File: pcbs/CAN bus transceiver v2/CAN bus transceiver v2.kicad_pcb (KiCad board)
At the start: 2 copper layers, 19.8 x 16 mm, 3 parts, among them P1 CONN_01X05, P2 CONN_01X02, U1 TCAN337GDR

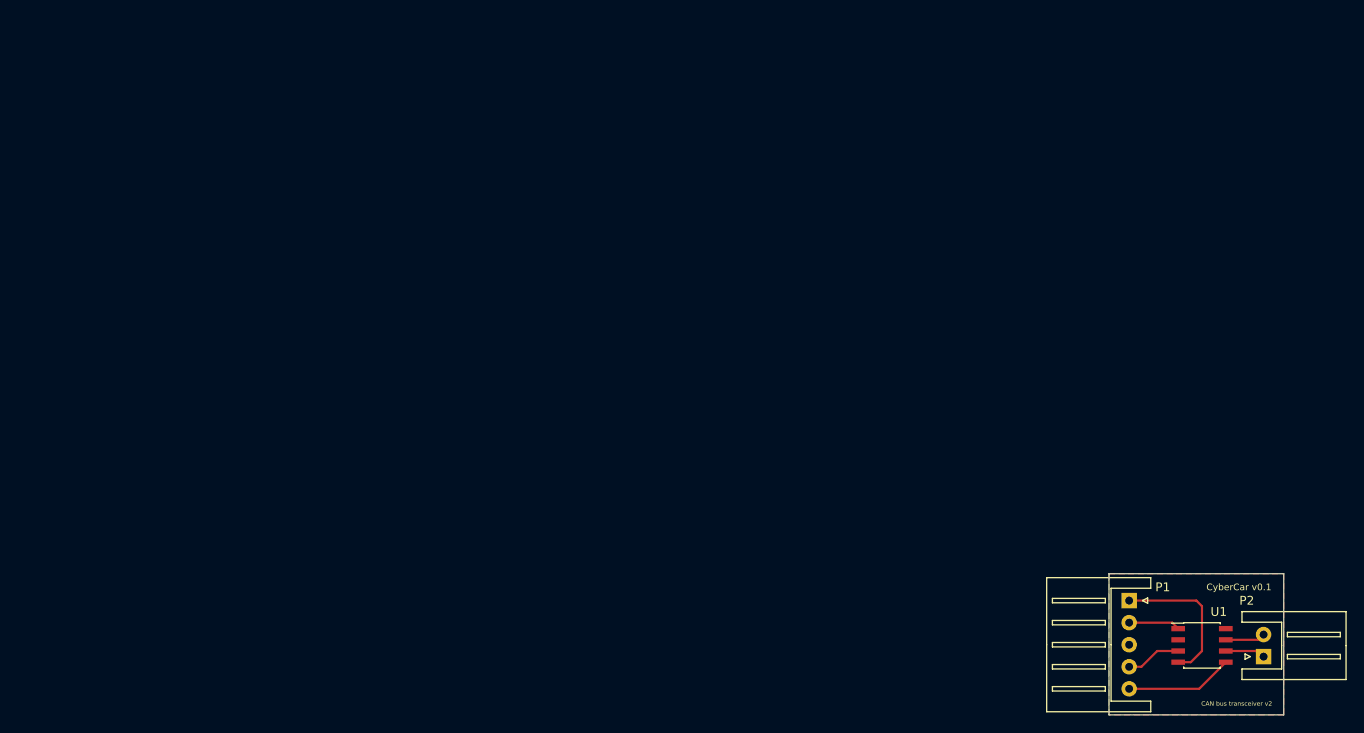
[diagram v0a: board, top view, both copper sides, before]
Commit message: added CAN bus transceiver
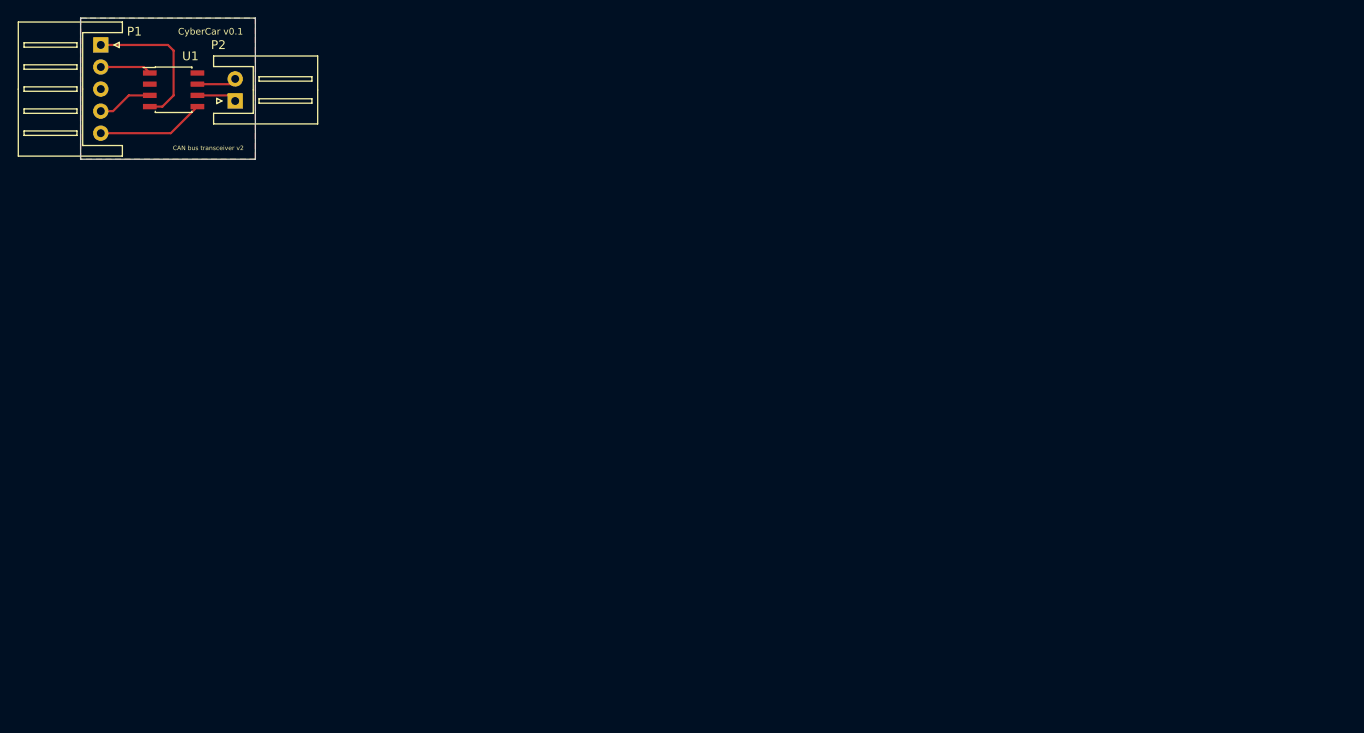
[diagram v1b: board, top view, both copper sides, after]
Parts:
- moved P1 132.5 mm to (29.5, 27.2)
- moved U1 132.5 mm to (37.7, 32.3)
- moved P2 132.5 mm to (44.7, 33.5)
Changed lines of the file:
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@@
     (links 8)
     (no_connects 0)
-    (area 134.775 86.994999 172.665 103.345001)
+    (area 18.189 16.35 65 40.353001)
     (thickness 1.6)
-    (drawings 13)
+    (drawings 15)
     (tracks 16)
     (zones 0)
@@
       (psnegative false)
       (psa4output false)
-      (plotreference true)
+      (plotreference false)
       (plotvalue false)
       (plotinvisibletext false)
@@
   )
   (module Connectors_JST:JST_XH_S05B-XH-A_05x2.50mm_Angled (layer F.Cu)
-    (at 146.05 90.17 270)
+    (at 29.464 27.178 270)
     (descr "JST XH series connector, S05B-XH-A, side entry type, through hole")
     (tags "connector jst xh tht side horizontal angled 2.50mm")
@@
   )
   (module Connectors_JST:JST_XH_S02B-XH-A_02x2.50mm_Angled (layer F.Cu)
-    (at 161.29 96.52 90)
+    (at 44.704 33.528 90)
     (descr "JST XH series connector, S02B-XH-A, side entry type, through hole")
     (tags "connector jst xh tht side horizontal angled 2.50mm")
@@
   )
   (module Housings_SOIC:SOIC-8_3.9x4.9mm_Pitch1.27mm (layer F.Cu)
-    (at 154.305 95.25)
+    (at 37.719 32.258)
     (descr "8-Lead Plastic Small Outline (SN) - Narrow, 3.90 mm Body [SOIC] (see Microchip Packaging Specification 00000049BS.pdf)")
     (tags "SOIC 1.27")
@@
     )
   )
-  (gr_line (start 163.576 103.124) (end 143.764 103.124) (angle 90) (layer Edge.Cuts) (width 0.1))
-  (gr_line (start 163.576 87.122) (end 163.576 103.124) (angle 90) (layer Edge.Cuts) (width 0.1))
-  (gr_line (start 143.764 87.122) (end 163.576 87.122) (angle 90) (layer Edge.Cuts) (width 0.1))
-  (gr_line (start 143.764 87.122) (end 143.764 103.124) (angle 90) (layer Edge.Cuts) (width 0.1))
-  (gr_text CANL (at 159.004 96.52) (layer B.SilkS)
-    (effects (font (size 0.5 0.5) (thickness 0.125)) (justify mirror))
-  )
-  (gr_text CANH (at 159.004 93.98) (layer B.SilkS)
-    (effects (font (size 0.5 0.5) (thickness 0.125)) (justify mirror))
-  )
-  (gr_text "CAN bus transceiver v2" (at 158.242 101.854) (layer F.SilkS)
+  (dimension 16.002 (width 0.3) (layer Dwgs.User)
+    (gr_text "16,002 mm" (at 58.5 32.131 270) (layer Dwgs.User)
+      (effects (font (size 1.5 1.5) (thickness 0.3)))
+    )
+    (feature1 (pts (xy 46.99 40.132) (xy 59.85 40.132)))
+    (feature2 (pts (xy 46.99 24.13) (xy 59.85 24.13)))
+    (crossbar (pts (xy 57.15 24.13) (xy 57.15 40.132)))
+    (arrow1a (pts (xy 57.15 40.132) (xy 56.563579 39.005496)))
+    (arrow1b (pts (xy 57.15 40.132) (xy 57.736421 39.005496)))
+    (arrow2a (pts (xy 57.15 24.13) (xy 56.563579 25.256504)))
+    (arrow2b (pts (xy 57.15 24.13) (xy 57.736421 25.256504)))
+  )
+  (dimension 19.812 (width 0.3) (layer Dwgs.User)
+    (gr_text "19,812 mm" (at 37.084 17.7) (layer Dwgs.User)
+      (effects (font (size 1.5 1.5) (thickness 0.3)))
+    )
+    (feature1 (pts (xy 46.99 24.13) (xy 46.99 16.35)))
+    (feature2 (pts (xy 27.178 24.13) (xy 27.178 16.35)))
+    (crossbar (pts (xy 27.178 19.05) (xy 46.99 19.05)))
+    (arrow1a (pts (xy 46.99 19.05) (xy 45.863496 19.636421)))
+    (arrow1b (pts (xy 46.99 19.05) (xy 45.863496 18.463579)))
+    (arrow2a (pts (xy 27.178 19.05) (xy 28.304504 19.636421)))
+    (arrow2b (pts (xy 27.178 19.05) (xy 28.304504 18.463579)))
+  )
+  (gr_line (start 46.99 40.132) (end 27.178 40.132) (angle 90) (layer Edge.Cuts) (width 0.1))
+  (gr_line (start 46.99 24.13) (end 46.99 40.132) (angle 90) (layer Edge.Cuts) (width 0.1))
+  (gr_line (start 27.178 24.13) (end 46.99 24.13) (angle 90) (layer Edge.Cuts) (width 0.1))
+  (gr_line (start 27.178 24.13) (end 27.178 40.132) (angle 90) (layer Edge.Cuts) (width 0.1))
+  (gr_text CANL (at 42.418 33.528) (layer B.SilkS)
+    (effects (font (size 0.5 0.5) (thickness 0.125)) (justify mirror))
+  )
+  (gr_text CANH (at 42.418 30.988) (layer B.SilkS)
+    (effects (font (size 0.5 0.5) (thickness 0.125)) (justify mirror))
+  )
+  (gr_text "CAN bus transceiver v2" (at 41.656 38.862) (layer F.SilkS)
     (effects (font (size 0.5 0.5) (thickness 0.125)))
   )
-  (gr_text "CyberCar v0.1" (at 158.496 88.646) (layer F.SilkS)
+  (gr_text "CyberCar v0.1" (at 41.91 25.654) (layer F.SilkS)
     (effects (font (size 0.75 0.75) (thickness 0.1875)))
   )
-  (gr_text RX (at 148.336 90.17) (layer B.SilkS)
-    (effects (font (size 0.5 0.5) (thickness 0.125)) (justify mirror))
-  )
-  (gr_text TX (at 148.336 92.71) (layer B.SilkS)
-    (effects (font (size 0.5 0.5) (thickness 0.125)) (justify mirror))
-  )
-  (gr_text GND (at 148.082 95.25) (layer B.SilkS)
-    (effects (font (size 0.5 0.5) (thickness 0.125)) (justify mirror))
-  )
-  (gr_text VCC (at 148.082 97.79) (layer B.SilkS)
-    (effects (font (size 0.5 0.5) (thickness 0.125)) (justify mirror))
-  )
-  (gr_text Fault (at 148.082 100.33) (layer B.SilkS)
-    (effects (font (size 0.5 0.5) (thickness 0.125)) (justify mirror))
-  )
-  (segment (start 151.605 97.155) (end 153.035 97.155) (width 0.25) (layer F.Cu) (net 1))
-  (segment (start 153.67 90.17) (end 146.05 90.17) (width 0.25) (layer F.Cu) (net 1))
-  (segment (start 154.305 90.805) (end 153.67 90.17) (width 0.25) (layer F.Cu) (net 1))
-  (segment (start 154.305 95.885) (end 154.305 90.805) (width 0.25) (layer F.Cu) (net 1))
-  (segment (start 153.035 97.155) (end 154.305 95.885) (width 0.25) (layer F.Cu) (net 1))
-  (segment (start 146.05 92.67) (end 150.93 92.67) (width 0.25) (layer F.Cu) (net 2))
-  (segment (start 150.93 92.67) (end 151.605 93.345) (width 0.25) (layer F.Cu) (net 2))
-  (segment (start 157.005 95.885) (end 160.655 95.885) (width 0.25) (layer F.Cu) (net 3) (status C00000))
-  (segment (start 160.655 95.885) (end 161.29 96.52) (width 0.25) (layer F.Cu) (net 3) (status C00000))
-  (segment (start 157.005 94.615) (end 160.695 94.615) (width 0.25) (layer F.Cu) (net 4) (status C00000))
-  (segment (start 160.695 94.615) (end 161.29 94.02) (width 0.25) (layer F.Cu) (net 4) (status C00000))
-  (segment (start 146.05 97.67) (end 147.44 97.67) (width 0.25) (layer F.Cu) (net 5))
-  (segment (start 149.225 95.885) (end 151.605 95.885) (width 0.25) (layer F.Cu) (net 5))
-  (segment (start 147.44 97.67) (end 149.225 95.885) (width 0.25) (layer F.Cu) (net 5))
-  (segment (start 146.05 100.17) (end 153.99 100.17) (width 0.25) (layer F.Cu) (net 7))
-  (segment (start 153.99 100.17) (end 157.005 97.155) (width 0.25) (layer F.Cu) (net 7))
+  (gr_text RX (at 31.75 27.178) (layer B.SilkS)
+    (effects (font (size 0.5 0.5) (thickness 0.125)) (justify mirror))
+  )
+  (gr_text TX (at 31.75 29.718) (layer B.SilkS)
+    (effects (font (size 0.5 0.5) (thickness 0.125)) (justify mirror))
+  )
+  (gr_text GND (at 31.496 32.258) (layer B.SilkS)
+    (effects (font (size 0.5 0.5) (thickness 0.125)) (justify mirror))
+  )
+  (gr_text VCC (at 31.496 34.798) (layer B.SilkS)
+    (effects (font (size 0.5 0.5) (thickness 0.125)) (justify mirror))
+  )
+  (gr_text Fault (at 31.496 37.338) (layer B.SilkS)
+    (effects (font (size 0.5 0.5) (thickness 0.125)) (justify mirror))
+  )
+  (segment (start 35.019 34.163) (end 36.449 34.163) (width 0.25) (layer F.Cu) (net 1))
+  (segment (start 37.084 27.178) (end 29.464 27.178) (width 0.25) (layer F.Cu) (net 1))
+  (segment (start 37.719 27.813) (end 37.084 27.178) (width 0.25) (layer F.Cu) (net 1))
+  (segment (start 37.719 32.893) (end 37.719 27.813) (width 0.25) (layer F.Cu) (net 1))
+  (segment (start 36.449 34.163) (end 37.719 32.893) (width 0.25) (layer F.Cu) (net 1))
+  (segment (start 29.464 29.678) (end 34.344 29.678) (width 0.25) (layer F.Cu) (net 2))
+  (segment (start 34.344 29.678) (end 35.019 30.353) (width 0.25) (layer F.Cu) (net 2))
+  (segment (start 40.419 32.893) (end 44.069 32.893) (width 0.25) (layer F.Cu) (net 3))
+  (segment (start 44.069 32.893) (end 44.704 33.528) (width 0.25) (layer F.Cu) (net 3))
+  (segment (start 40.419 31.623) (end 44.109 31.623) (width 0.25) (layer F.Cu) (net 4))
+  (segment (start 44.109 31.623) (end 44.704 31.028) (width 0.25) (layer F.Cu) (net 4))
+  (segment (start 29.464 34.678) (end 30.854 34.678) (width 0.25) (layer F.Cu) (net 5))
+  (segment (start 32.639 32.893) (end 35.019 32.893) (width 0.25) (layer F.Cu) (net 5))
+  (segment (start 30.854 34.678) (end 32.639 32.893) (width 0.25) (layer F.Cu) (net 5))
+  (segment (start 29.464 37.178) (end 37.404 37.178) (width 0.25) (layer F.Cu) (net 7))
+  (segment (start 37.404 37.178) (end 40.419 34.163) (width 0.25) (layer F.Cu) (net 7))
   (zone (net 6) (net_name GND) (layer F.Cu) (hatch edge 0.508)
     (connect_pads (clearance 0.508))
@@
     (polygon
       (pts
-        (xy 163.576 103.124) (xy 143.764 103.124) (xy 143.764 87.122) (xy 163.576 87.122)
+        (xy 46.99 40.132) (xy 27.178 40.132) (xy 27.178 24.13) (xy 46.99 24.13)
       )
     )
